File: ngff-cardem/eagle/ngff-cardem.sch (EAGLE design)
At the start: 145 parts, among them IC1 FPF2109, IC2 FPF2109, IC201 CB3Q3244PW, IC202 CB3Q3244PW, IC203 IP4234CZ6, IC301 MCP1703CB, IC302 TPS22958-DGN, J301 PJ-002BH-SMT-TR, M2 MENTOR_12701001, M3 MENTOR_12701001, Q201 12MHz, T101 BC847, U201 IP4234CZ6, U202 AT91SAM3S-AU, U301 MIC5366-1.8YC5, X1 PINHD-2X3-SP, X102 ZX360D-B-10P(30), X2 PINHD-2X3-SP, X201 MINI-USB-SHIELD-UX60-MB-5ST, X202 2.54mm, X301 22-23-2041

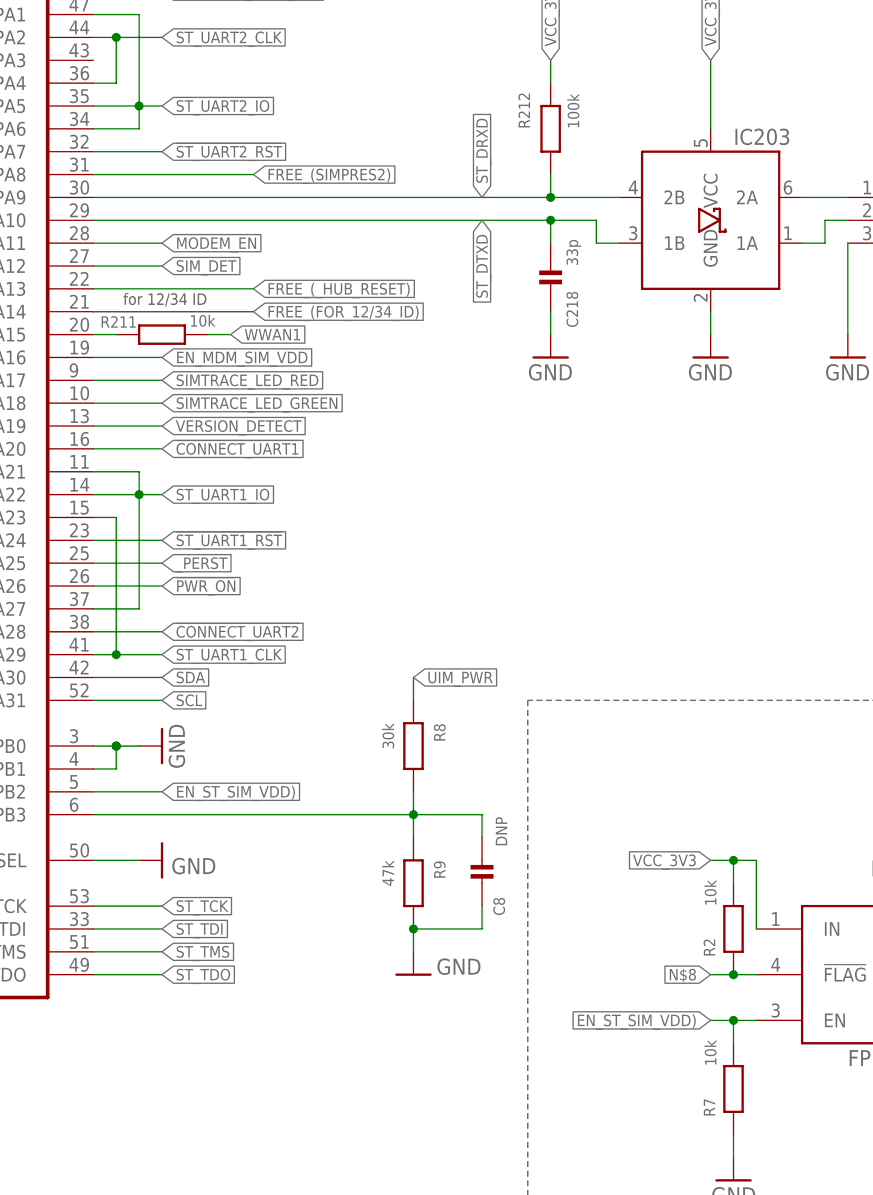
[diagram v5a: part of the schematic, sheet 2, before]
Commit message: ngff-cardem: bring /FLAG of IC1 to a GPIO (solves SYS#5477)
GPIO is PA8 (former QMOD's 'SIMPRES2').

Note, that the OCP of the FPF2109 is 200mA; there is no 100mA version
in this series and w/ 1V8 lowest Vin.
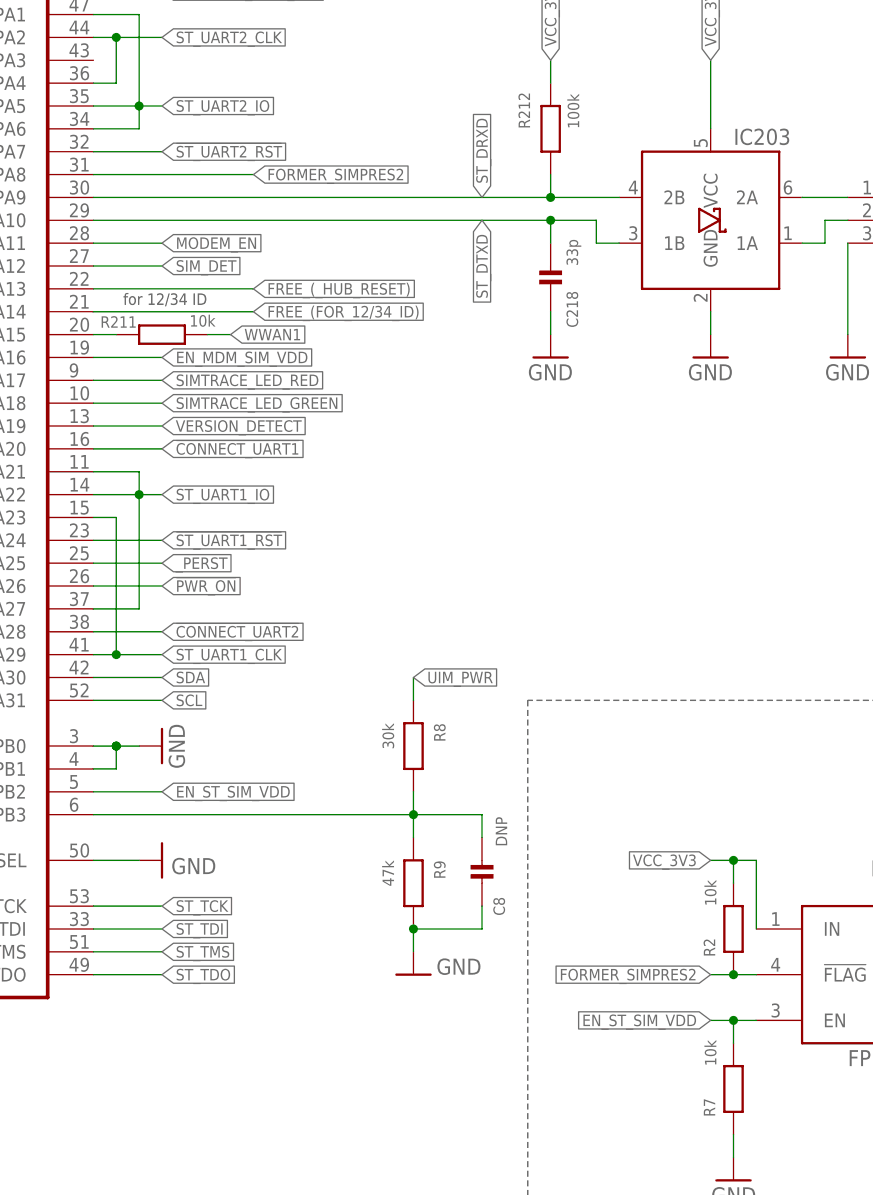
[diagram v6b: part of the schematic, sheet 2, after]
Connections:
- net EN_ST_SIM_VDD) renamed EN_ST_SIM_VDD
- removed net FREE_(SIMPRES2): U202.PGMM0/XOUT32/CTS0/PA8
- removed net N$8: IC1.!FLAG, R2.2
- new net FORMER_SIMPRES2: IC1.!FLAG, R2.2, U202.PGMM0/XOUT32/CTS0/PA8
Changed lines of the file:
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@@
 </segment>
 </net>
-<net name="FREE_(SIMPRES2)" class="0">
+<net name="FORMER_SIMPRES2" class="0">
 <segment>
 <pinref part="U202" gate="G$1" pin="PGMM0/XOUT32/CTS0/PA8"/>
 <wire x1="205.74" y1="210.82" x2="223.52" y2="210.82" width="0.1524" layer="91"/>
 <label x="223.52" y="210.82" size="1.27" layer="95" xref="yes"/>
+</segment>
+<segment>
+<pinref part="IC1" gate="U$1" pin="!FLAG"/>
+<wire x1="279.4" y1="121.92" x2="276.86" y2="121.92" width="0.1524" layer="91"/>
+<label x="274.32" y="121.92" size="1.27" layer="95" rot="R180" xref="yes"/>
+<pinref part="R2" gate="G$1" pin="2"/>
+<wire x1="276.86" y1="121.92" x2="274.32" y2="121.92" width="0.1524" layer="91"/>
+<junction x="276.86" y="121.92"/>
 </segment>
 </net>
@@
 </segment>
 </net>
-<net name="EN_ST_SIM_VDD)" class="0">
+<net name="EN_ST_SIM_VDD" class="0">
 <segment>
 <pinref part="U202" gate="G$1" pin="URXD1/AD6/PB2"/>
@@
 </segment>
 </net>
-<net name="N$8" class="0">
-<segment>
-<pinref part="IC1" gate="U$1" pin="!FLAG"/>
-<wire x1="279.4" y1="121.92" x2="276.86" y2="121.92" width="0.1524" layer="91"/>
-<label x="274.32" y="121.92" size="1.27" layer="95" rot="R180" xref="yes"/>
-<pinref part="R2" gate="G$1" pin="2"/>
-<wire x1="276.86" y1="121.92" x2="274.32" y2="121.92" width="0.1524" layer="91"/>
-<junction x="276.86" y="121.92"/>
-</segment>
-</net>

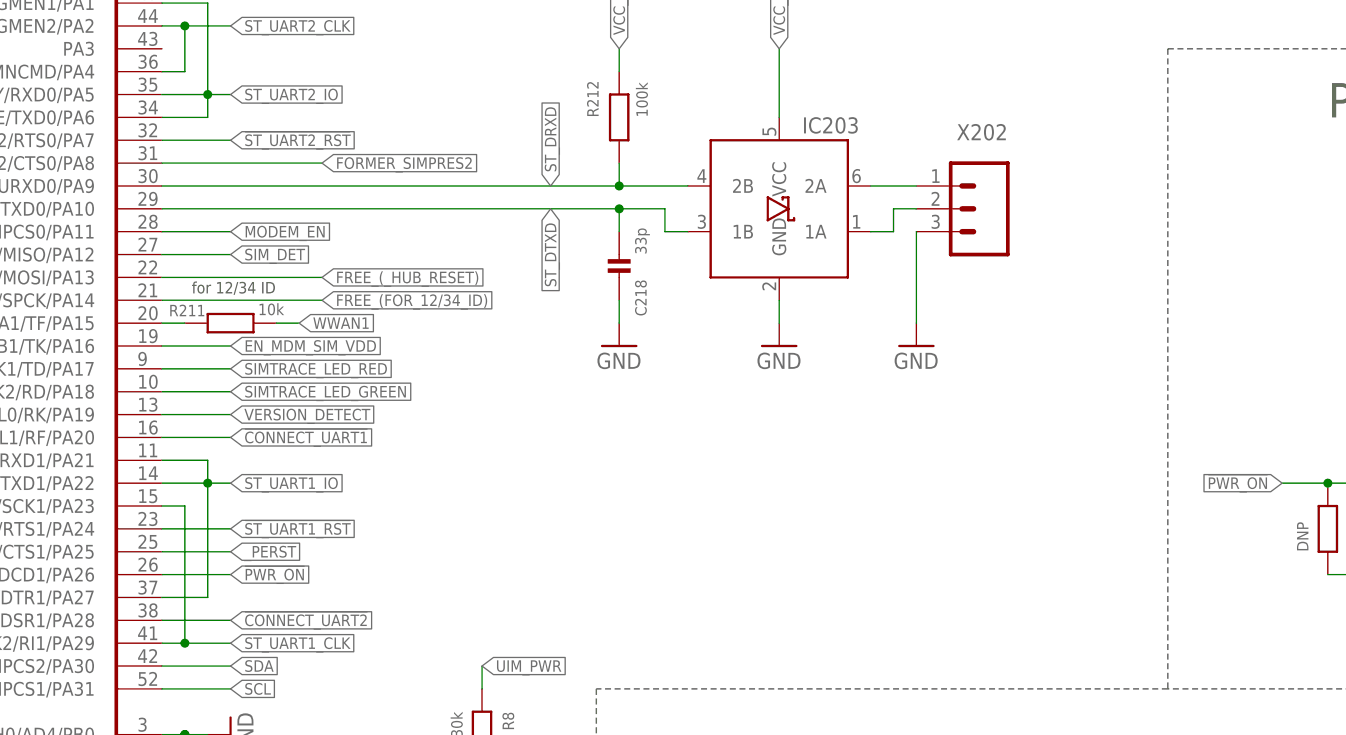
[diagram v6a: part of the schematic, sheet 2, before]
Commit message: ngff-cardem: add series 47R into SAM3S' RxD line (PA9) (solves SYS#5470)
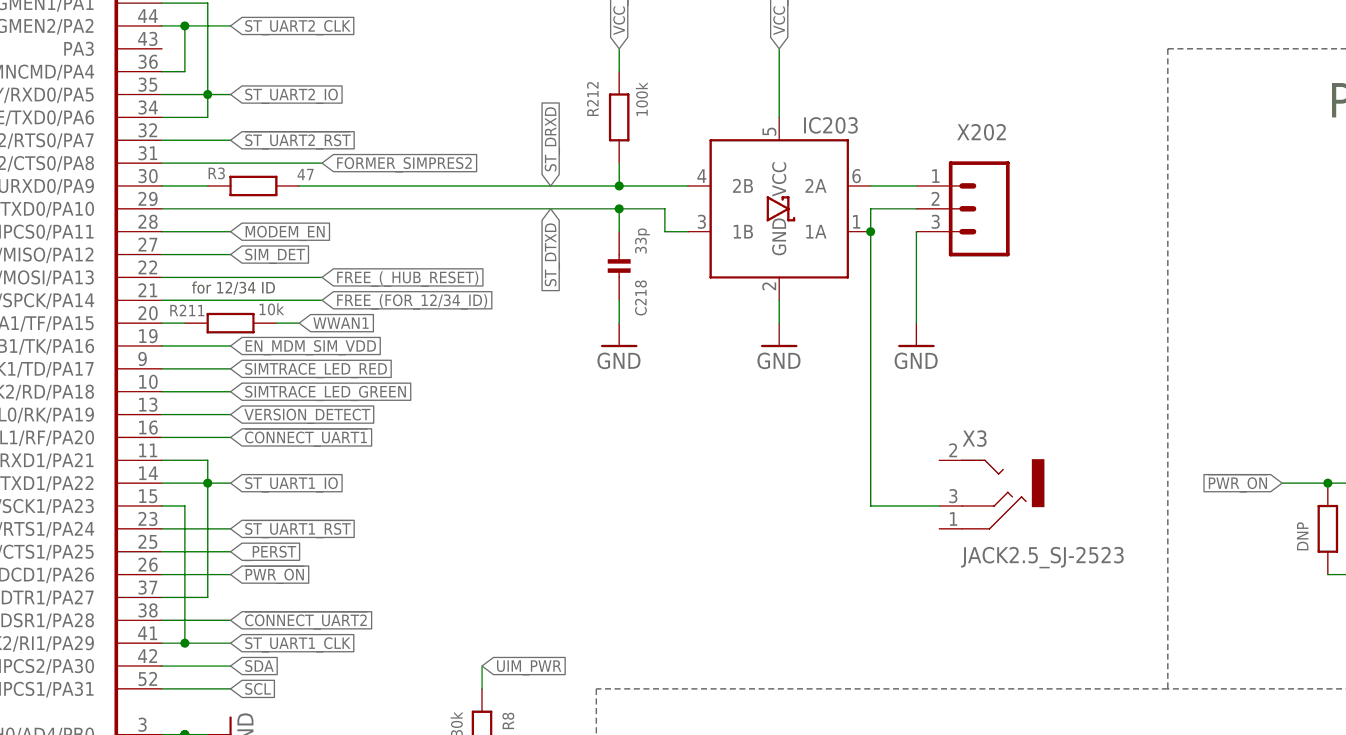
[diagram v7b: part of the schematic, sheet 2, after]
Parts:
- added R3: 47, rc-sysmocom:RESISTOR_0402
- added X3: JACK2.5_SJ-2523, laforge:JACK2.5_SJ-2523
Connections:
- removed net N$75: IC203.1A, X202.2
- new net N$8: R3.1, U202.NPCS1/URXD0/PA9
- new net UART_TX0: IC203.1A, X202.2, X3.MIDDLE
- net ST_DRXD: now also R3.2; no longer U202.NPCS1/URXD0/PA9
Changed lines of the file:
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@@
 <layer number="97" name="Info" color="7" fill="1" visible="yes" active="yes"/>
 <layer number="98" name="Guide" color="6" fill="1" visible="yes" active="yes"/>
+<layer number="99" name="SpiceOrder" color="7" fill="1" visible="no" active="no"/>
+<layer number="100" name="Muster" color="7" fill="1" visible="no" active="no"/>
+<layer number="200" name="200bmp" color="1" fill="10" visible="no" active="no"/>
+<layer number="217" name="217bmp" color="18" fill="1" visible="no" active="no"/>
+<layer number="218" name="218bmp" color="19" fill="1" visible="no" active="no"/>
+<layer number="219" name="219bmp" color="20" fill="1" visible="no" active="no"/>
+<layer number="220" name="220bmp" color="21" fill="1" visible="no" active="no"/>
+<layer number="221" name="221bmp" color="22" fill="1" visible="no" active="no"/>
+<layer number="222" name="222bmp" color="23" fill="1" visible="no" active="no"/>
+<layer number="223" name="223bmp" color="24" fill="1" visible="no" active="no"/>
+<layer number="224" name="224bmp" color="25" fill="1" visible="no" active="no"/>
+<layer number="250" name="Descript" color="3" fill="1" visible="no" active="no"/>
+<layer number="251" name="SMDround" color="12" fill="11" visible="no" active="no"/>
 </layers>
 <schematic xreflabel="%F%N/%S.%C%R" xrefpart="/%S.%C%R">
@@
 <attribute name="SOURCEPARTNUMBER" value="RNCP0603FTD10K0CT-ND"/>
 </part>
+<part name="X3" library="laforge" deviceset="JACK2.5_SJ-2523" device="">
+<attribute name="CLASS" value="CONNECTOR"/>
+<attribute name="DESCRIPTION" value="CONN JACK STEREO 2.5MM SMD R/A"/>
+<attribute name="LINK" value="https://www.digikey.de/product-detail/de/cui-inc/SJ-2523-SMT-TR/CP-2523SJCT-ND/669702"/>
+<attribute name="MANUFACTURER" value="CUI Inc."/>
+<attribute name="MANUFACTURERPARTNUMBER" value="SJ-2523-SMT-TR"/>
+<attribute name="POPULATED" value="TRUE"/>
+<attribute name="ROHSCERTIFICATE" value="Bleifrei / RoHS-konform"/>
+<attribute name="SOURCE" value="DIGIKEY"/>
+<attribute name="SOURCEPARTNUMBER" value="CP-2523SJCT-ND"/>
+</part>
+<part name="R3" library="rc-sysmocom" deviceset="RESISTOR" device="_0402" value="47">
+<attribute name="CLASS" value="RESISTOR"/>
+<attribute name="DESCRIPTION" value="RES SMD 47R 0402 1%"/>
+<attribute name="LINK" value="https://www.digikey.de/product-detail/de/te-connectivity-passive-product/CRGCQ0402F47R/A129611CT-ND"/>
+<attribute name="MANUFACTURER" value="TE Connectivity Passive Product"/>
+<attribute name="MANUFACTURERPARTNUMBER" value="CRGCQ0402F47R"/>
+<attribute name="POPULATED" value="TRUE"/>
+<attribute name="ROHSCERTIFICATE" value="Bleifrei / RoHS-konform"/>
+<attribute name="SOURCE" value="DIGIKEY"/>
+<attribute name="SOURCEPARTNUMBER" value="A129611CT-ND"/>
+</part>
 </parts>
 <sheets>
@@
 <attribute name="LINK" x="276.86" y="127" size="1.778" layer="96" rot="R180" display="off"/>
 </instance>
+<instance part="X3" gate="G$1" x="297.18" y="175.26">
+<attribute name="DESCRIPTION" x="297.18" y="175.26" size="1.778" layer="96" display="off"/>
+<attribute name="MANUFACTURER" x="297.18" y="175.26" size="1.778" layer="96" display="off"/>
+<attribute name="MANUFACTURERPARTNUMBER" x="297.18" y="175.26" size="1.778" layer="96" display="off"/>
+<attribute name="SOURCE" x="297.18" y="175.26" size="1.778" layer="96" display="off"/>
+<attribute name="SOURCEPARTNUMBER" x="297.18" y="175.26" size="1.778" layer="96" display="off"/>
+<attribute name="ROHSCERTIFICATE" x="297.18" y="175.26" size="1.778" layer="96" display="off"/>
+<attribute name="POPULATED" x="297.18" y="175.26" size="1.778" layer="96" display="off"/>
+<attribute name="CLASS" x="297.18" y="175.26" size="1.778" layer="96" display="off"/>
+<attribute name="LINK" x="297.18" y="175.26" size="1.778" layer="96" display="off"/>
+</instance>
+<instance part="R3" gate="G$1" x="215.9" y="208.28" smashed="yes">
+<attribute name="NAME" x="212.852" y="210.312" size="1.27" layer="95" rot="R180"/>
+<attribute name="VALUE" x="220.726" y="208.915" size="1.27" layer="96"/>
+<attribute name="DESCRIPTION" x="215.9" y="208.28" size="1.778" layer="96" rot="R180" display="off"/>
+<attribute name="MANUFACTURER" x="215.9" y="208.28" size="1.778" layer="96" rot="R180" display="off"/>
+<attribute name="MANUFACTURERPARTNUMBER" x="215.9" y="208.28" size="1.778" layer="96" rot="R180" display="off"/>
+<attribute name="SOURCE" x="215.9" y="208.28" size="1.778" layer="96" rot="R180" display="off"/>
+<attribute name="SOURCEPARTNUMBER" x="215.9" y="208.28" size="1.778" layer="96" rot="R180" display="off"/>
+<attribute name="ROHSCERTIFICATE" x="215.9" y="208.28" size="1.778" layer="96" rot="R180" display="off"/>
+<attribute name="POPULATED" x="215.9" y="208.28" size="1.778" layer="96" rot="R180" display="off"/>
+<attribute name="CLASS" x="215.9" y="208.28" size="1.778" layer="96" rot="R180" display="off"/>
+<attribute name="LINK" x="215.9" y="208.28" size="1.778" layer="96" rot="R180" display="off"/>
+</instance>
 </instances>
 <busses>
@@
 <pinref part="R212" gate="G$1" pin="1"/>
 <wire x1="256.54" y1="210.82" x2="256.54" y2="208.28" width="0.1524" layer="91"/>
-<pinref part="U202" gate="G$1" pin="NPCS1/URXD0/PA9"/>
-<wire x1="205.74" y1="208.28" x2="256.54" y2="208.28" width="0.1524" layer="91"/>
 <label x="248.92" y="208.28" size="1.27" layer="95" rot="R90" xref="yes"/>
-<junction x="256.54" y="208.28"/>
 <pinref part="IC203" gate="G$1" pin="2B"/>
 <wire x1="256.54" y1="208.28" x2="264.16" y2="208.28" width="0.1524" layer="91"/>
+<pinref part="R3" gate="G$1" pin="2"/>
+<wire x1="220.98" y1="208.28" x2="256.54" y2="208.28" width="0.1524" layer="91"/>
+<junction x="256.54" y="208.28"/>
 </segment>
 </net>
@@
 </segment>
 </net>
-<net name="N$75" class="0">
-<segment>
-<pinref part="IC203" gate="G$1" pin="1A"/>
-<wire x1="284.48" y1="203.2" x2="287.02" y2="203.2" width="0.1524" layer="91"/>
-<wire x1="287.02" y1="203.2" x2="287.02" y2="205.74" width="0.1524" layer="91"/>
-<pinref part="X202" gate="G$1" pin="2"/>
-<wire x1="287.02" y1="205.74" x2="289.56" y2="205.74" width="0.1524" layer="91"/>
-</segment>
-</net>
 <net name="VCC_3V3" class="2">
 <segment>
@@
 </segment>
 </net>
+<net name="UART_TX0" class="0">
+<segment>
+<pinref part="X3" gate="G$1" pin="MIDDLE"/>
+<wire x1="284.48" y1="172.72" x2="292.1" y2="172.72" width="0.1524" layer="91"/>
+<pinref part="IC203" gate="G$1" pin="1A"/>
+<wire x1="284.48" y1="172.72" x2="284.48" y2="203.2" width="0.1524" layer="91"/>
+<pinref part="X202" gate="G$1" pin="2"/>
+<wire x1="289.56" y1="205.74" x2="284.48" y2="205.74" width="0.1524" layer="91"/>
+<wire x1="284.48" y1="205.74" x2="284.48" y2="203.2" width="0.1524" layer="91"/>
+<junction x="284.48" y="203.2"/>
+</segment>
+</net>
+<net name="N$8" class="0">
+<segment>
+<pinref part="R3" gate="G$1" pin="1"/>
+<pinref part="U202" gate="G$1" pin="NPCS1/URXD0/PA9"/>
+<wire x1="210.82" y1="208.28" x2="205.74" y2="208.28" width="0.1524" layer="91"/>
+</segment>
+</net>
